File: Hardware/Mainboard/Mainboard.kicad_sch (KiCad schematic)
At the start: 0 parts

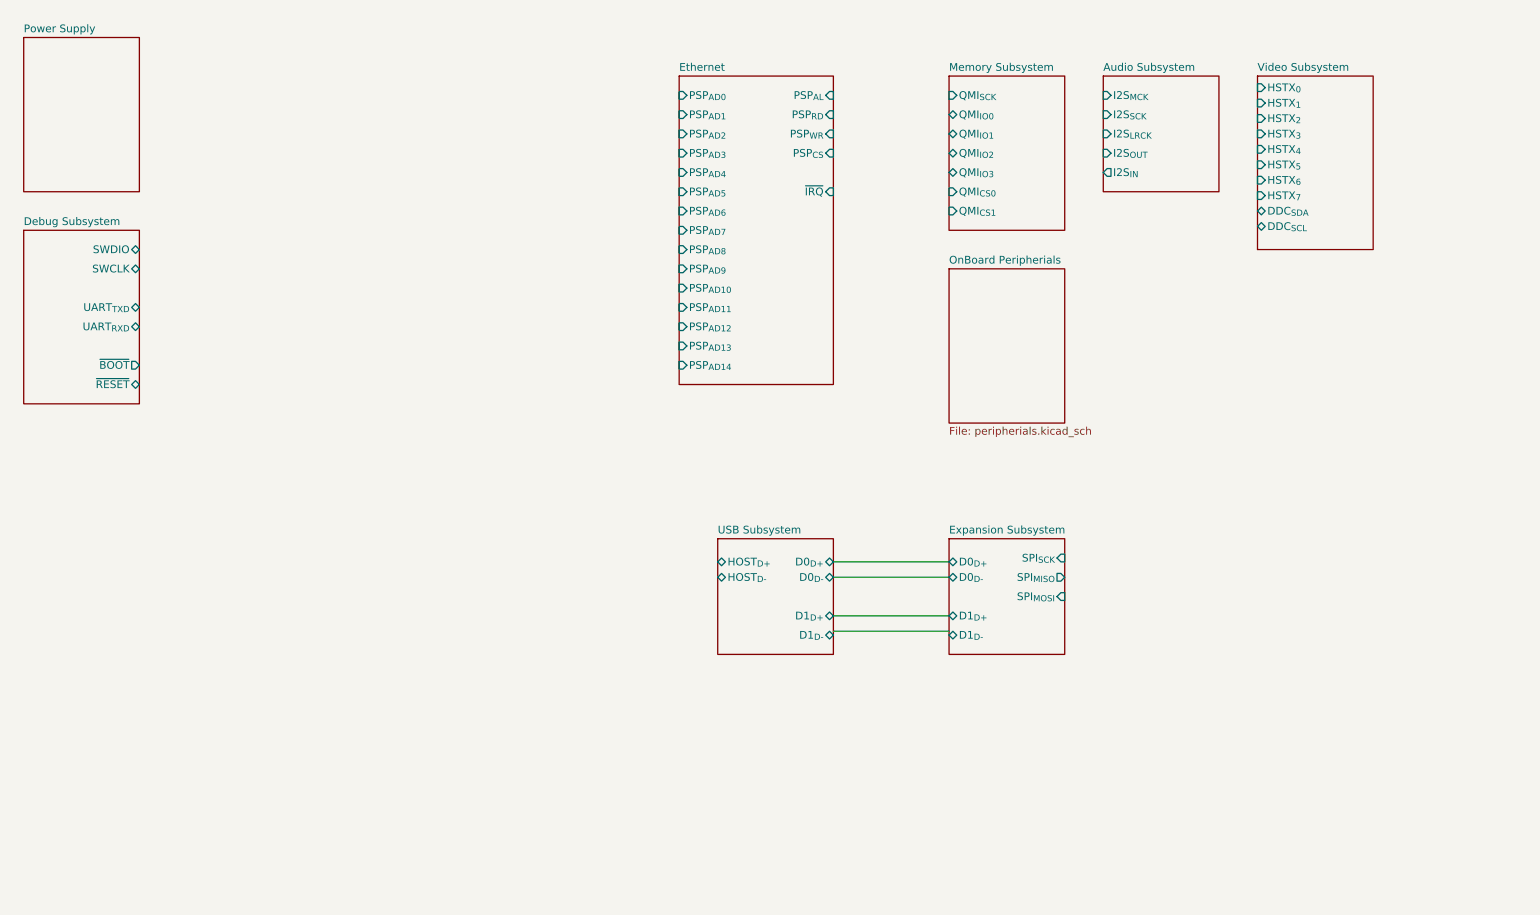
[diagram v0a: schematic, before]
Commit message: Adds more work on the mainboard schematic
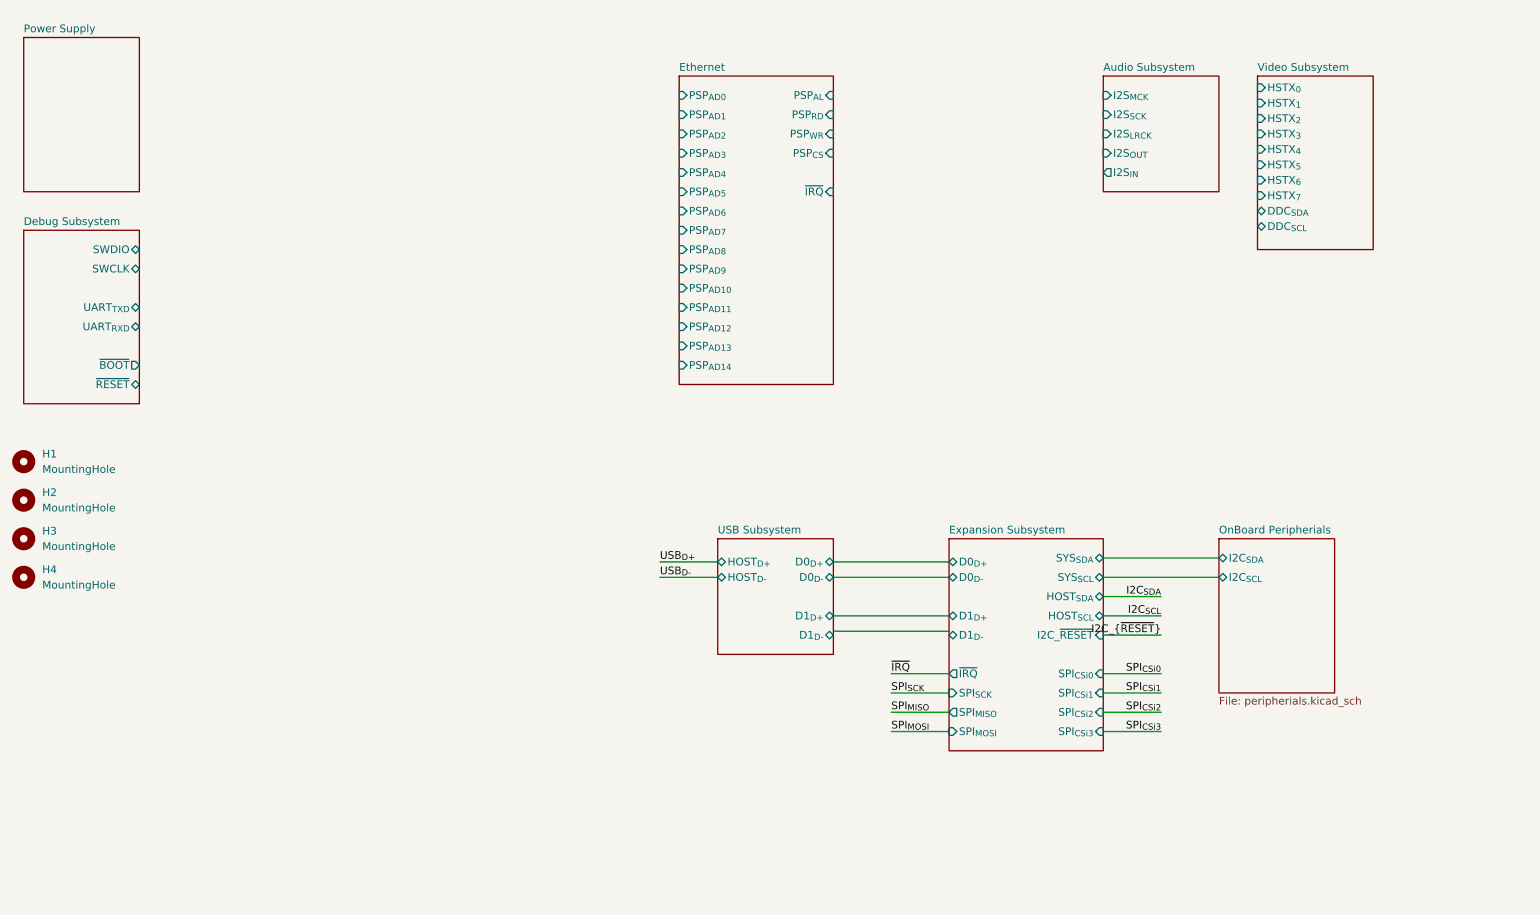
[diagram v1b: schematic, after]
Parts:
- added H1, H2, H3, H4: MountingHole, MountingHole:MountingHole_4.3mm_M4_Pad_Via, symbol Mechanical:MountingHole
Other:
- removed sheet Memory Subsystem
- sheet Expansion Subsystem ports: added HOST_{SCL}, HOST_{SDA}, I2C_~{RESET}, SPI_{CSi0}, SPI_{CSi1}, SPI_{CSi2}, SPI_{CSi3}, SYS_{SCL}, SYS_{SDA}, ~{IRQ}; removed none
- sheet OnBoard Peripherials ports: added I2C_{SCL}, I2C_{SDA}; removed none

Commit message: Adds RP2350 Stamp XL and dummy expansion board
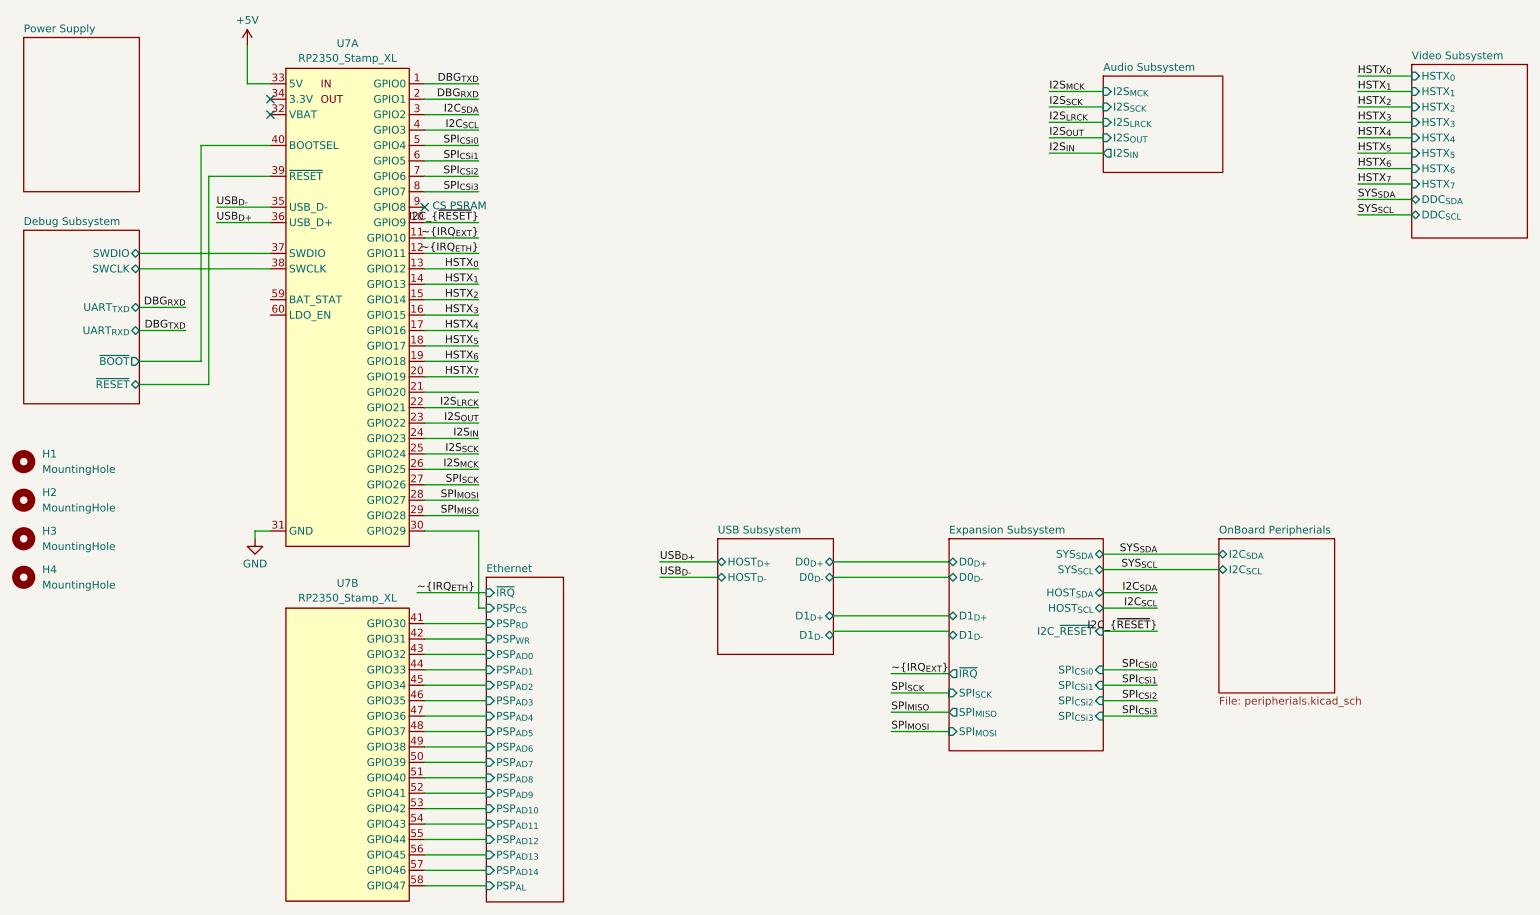
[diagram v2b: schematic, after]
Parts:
- added U7: RP2350_Stamp_XL, RP2xxx_Stamp:RP2xxx_Stamp_XL_FlexyPin, symbol RP2xxx_Stamp:RP2350_Stamp_XL
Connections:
- net Debug Subsystem/SWCLK: now also U7.38 (SWCLK)
- net Debug Subsystem/SWDIO: now also U7.37 (SWDIO)
- net Debug Subsystem/~{BOOT}: now also U7.40 (BOOTSEL)
- net Debug Subsystem/~{RESET}: now also U7.39 (~{RESET})
- net Ethernet/PSP_{AD0}: now also U7.43 (GPIO32)
- net Ethernet/PSP_{AD10}: now also U7.53 (GPIO42)
- net Ethernet/PSP_{AD11}: now also U7.54 (GPIO43)
- net Ethernet/PSP_{AD12}: now also U7.55 (GPIO44)
- net Ethernet/PSP_{AD13}: now also U7.56 (GPIO45)
- net Ethernet/PSP_{AD14}: now also U7.57 (GPIO46)
- net Ethernet/PSP_{AD1}: now also U7.44 (GPIO33)
- net Ethernet/PSP_{AD2}: now also U7.45 (GPIO34)
- net Ethernet/PSP_{AD3}: now also U7.46 (GPIO35)
- net Ethernet/PSP_{AD4}: now also U7.47 (GPIO36)
- net Ethernet/PSP_{AD5}: now also U7.48 (GPIO37)
- net Ethernet/PSP_{AD6}: now also U7.49 (GPIO38)
- net Ethernet/PSP_{AD7}: now also U7.50 (GPIO39)
- net Ethernet/PSP_{AD8}: now also U7.51 (GPIO40)
- net Ethernet/PSP_{AD9}: now also U7.52 (GPIO41)
- net Ethernet/PSP_{AL}: now also U7.58 (GPIO47)
- net Ethernet/PSP_{CS}: now also U7.30 (GPIO29)
- net Ethernet/PSP_{RD}: now also U7.41 (GPIO30)
- net Ethernet/PSP_{WR}: now also U7.42 (GPIO31)
- net I2C_{SCL}: now also U7.4 (GPIO3)
- net I2C_{SDA}: now also U7.3 (GPIO2)
- net I2C_{~{RESET}}: now also U7.10 (GPIO9)
- net SPI_{CSi0}: now also U7.5 (GPIO4)
- net SPI_{CSi1}: now also U7.6 (GPIO5)
- net SPI_{CSi2}: now also U7.7 (GPIO6)
- net SPI_{CSi3}: now also U7.8 (GPIO7)
- net SPI_{MISO}: now also U7.29 (GPIO28)
- net SPI_{MOSI}: now also U7.28 (GPIO27)
- net SPI_{SCK}: now also U7.27 (GPIO26)
- net USB_{D+}: now also U7.36 (USB_D+)
- net USB_{D-}: now also U7.35 (USB_D-)
- new net +5V: U7.33 (5V)
- new net DBG_{RXD}: U7.2 (GPIO1)
- new net DBG_{TXD}: U7.1 (GPIO0)
- new net GND: U7.31 (GND)
- new net HSTX_{0}: U7.13 (GPIO12)
- new net HSTX_{1}: U7.14 (GPIO13)
- new net HSTX_{2}: U7.15 (GPIO14)
- new net HSTX_{3}: U7.16 (GPIO15)
- new net HSTX_{4}: U7.17 (GPIO16)
- new net HSTX_{5}: U7.18 (GPIO17)
- new net HSTX_{6}: U7.19 (GPIO18)
- new net HSTX_{7}: U7.20 (GPIO19)
- new net I2S_{IN}: U7.24 (GPIO23)
- new net I2S_{LRCK}: U7.22 (GPIO21)
- new net I2S_{MCK}: U7.26 (GPIO25)
- new net I2S_{OUT}: U7.23 (GPIO22)
- new net I2S_{SCK}: U7.25 (GPIO24)
- new net ~{IRQ_{ETH}}: U7.12 (GPIO11)
- new net ~{IRQ_{EXT}}: U7.11 (GPIO10)
- no-connect marks 0 -> 3
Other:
- note added: "CS PSRAM"

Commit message: More work on the motherboard
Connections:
- net Ethernet/PSP_{AL}: now also U7.42 (GPIO31); no longer U7.58 (GPIO47)
- net Ethernet/PSP_{CS}: now also U7.58 (GPIO47); no longer U7.30 (GPIO29)
- net Ethernet/PSP_{WR}: now also U7.30 (GPIO29); no longer U7.42 (GPIO31)
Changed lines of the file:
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@@
 		)
 		(pin "PSP_{CS}" input
-			(at 95.25 113.03 180)
+			(at 95.25 158.75 180)
 			(effects
 				(font
@@
 		)
 		(pin "PSP_{AL}" input
-			(at 95.25 158.75 180)
+			(at 95.25 118.11 180)
 			(effects
 				(font
@@
 		)
 		(pin "PSP_{WR}" input
-			(at 95.25 118.11 180)
+			(at 95.25 113.03 180)
 			(effects
 				(font
